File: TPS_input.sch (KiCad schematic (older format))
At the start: 3 parts, among them P48 CONN_1, P49 CONN_1, P50 CONN_1

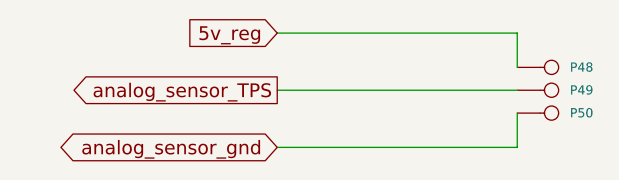
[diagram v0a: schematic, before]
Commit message: Removed LM1815 options. Now adaptive mode and square waves are the default,
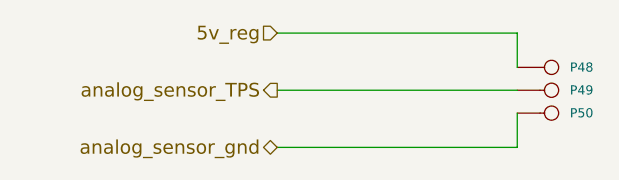
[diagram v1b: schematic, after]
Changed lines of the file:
@@
-EESchema Schematic File Version 1
-LIBS:power,./freeEMS_lib,device,conn,linear,regul,74xx,cmos4000,adc-dac,memory,xilinx,special,microcontrollers,dsp,microchip,analog_switches,motorola,texas,intel,audio,interface,digital-audio,philips,display,cypress,siliconi,contrib,valves,./freeEMS_1.cache
+EESchema Schematic File Version 2  date Fri 02 Jul 2010 02:24:35 PM ART
+LIBS:power
+LIBS:freeEMS_lib
+LIBS:device
+LIBS:conn
+LIBS:linear
+LIBS:regul
+LIBS:74xx
+LIBS:cmos4000
+LIBS:adc-dac
+LIBS:memory
+LIBS:xilinx
+LIBS:special
+LIBS:microcontrollers
+LIBS:dsp
+LIBS:microchip
+LIBS:analog_switches
+LIBS:motorola
+LIBS:texas
+LIBS:intel
+LIBS:audio
+LIBS:interface
+LIBS:digital-audio
+LIBS:philips
+LIBS:display
+LIBS:cypress
+LIBS:siliconi
+LIBS:contrib
+LIBS:valves
+LIBS:freeEMS_1-cache
 EELAYER 23  0
 EELAYER END
@@
 Sheet 38 41
 Title "freeEMS 1.0"
-Date "15 nov 2008"
+Date "2 jul 2010"
 Rev "A.20"
 Comp "diyefi.org"
@@
 U 1 1 48AA1ACF
 P 4450 2050
-F 0 "P50" H 4530 2050 40  0000 L C
-F 1 "CONN_1" H 4450 2105 30  0001 C C
-F 2 "1PIN" V 1130 2600 60  0001 C C
+F 0 "P50" H 4530 2050 40  0000 L CNN
+F 1 "CONN_1" H 4450 2105 30  0001 C CNN
+F 2 "1PIN" V 1130 2600 60  0001 C CNN
 	1    4450 2050
 	1    0    0    -1
@@
 U 1 1 48AA1ACC
 P 4450 1950
-F 0 "P49" H 4530 1950 40  0000 L C
-F 1 "CONN_1" H 4450 2005 30  0001 C C
-F 2 "1PIN" V 1130 2600 60  0001 C C
+F 0 "P49" H 4530 1950 40  0000 L CNN
+F 1 "CONN_1" H 4450 2005 30  0001 C CNN
+F 2 "1PIN" V 1130 2600 60  0001 C CNN
 	1    4450 1950
 	1    0    0    -1
@@
 U 1 1 48AA1AC9
 P 4450 1850
-F 0 "P48" H 4530 1850 40  0000 L C
-F 1 "CONN_1" H 4450 1905 30  0001 C C
-F 2 "1PIN" V 1130 2600 60  0001 C C
+F 0 "P48" H 4530 1850 40  0000 L CNN
+F 1 "CONN_1" H 4450 1905 30  0001 C CNN
+F 2 "1PIN" V 1130 2600 60  0001 C CNN
 	1    4450 1850
 	1    0    0    -1
@@
 Wire Wire Line
 	4300 1700 4300 1850
-Text GLabel 3250 1700 0    60   Input
+Text HLabel 3250 1700 0    60   Input ~ 0
 5v_reg
-Text GLabel 3250 2200 0    60   BiDi
+Text HLabel 3250 2200 0    60   BiDi ~ 0
 analog_sensor_gnd
-Text GLabel 3250 1950 0    60   Output
+Text HLabel 3250 1950 0    60   Output ~ 0
 analog_sensor_TPS
 $EndSCHEMATC

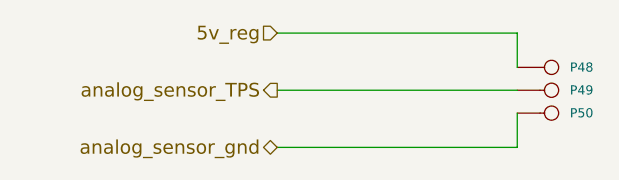
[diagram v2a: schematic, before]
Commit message: Implemented P&H, removed current sense circuitry, removed all unnecessary files from the repo
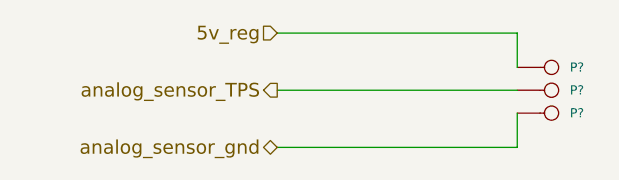
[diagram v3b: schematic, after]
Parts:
- renumbered P48 to P?, P49 to P?, P50 to P?
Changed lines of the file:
@@
-EESchema Schematic File Version 2  date Fri 02 Jul 2010 05:44:26 PM ART
+EESchema Schematic File Version 2  date Sat 03 Jul 2010 10:49:02 AM ART
 LIBS:power
 LIBS:freeEMS_lib
@@
 EELAYER END
 $Descr A4 11700 8267
-Sheet 38 41
+Sheet 39 41
 Title "freeEMS 1.0"
-Date "2 jul 2010"
-Rev "A.20"
+Date "3 jul 2010"
+Rev "A.08"
 Comp "diyefi.org"
 Comment1 "TPS_input.sch"
@@
 $EndDescr
 $Comp
-L CONN_1 P50
+L CONN_1 P?
 U 1 1 48AA1ACF
 P 4450 2050
-F 0 "P50" H 4530 2050 40  0000 L CNN
+F 0 "P?" H 4530 2050 40  0000 L CNN
 F 1 "CONN_1" H 4450 2105 30  0001 C CNN
 F 2 "1PIN" V 1130 2600 60  0001 C CNN
@@
 $EndComp
 $Comp
-L CONN_1 P49
+L CONN_1 P?
 U 1 1 48AA1ACC
 P 4450 1950
-F 0 "P49" H 4530 1950 40  0000 L CNN
+F 0 "P?" H 4530 1950 40  0000 L CNN
 F 1 "CONN_1" H 4450 2005 30  0001 C CNN
 F 2 "1PIN" V 1130 2600 60  0001 C CNN
@@
 $EndComp
 $Comp
-L CONN_1 P48
+L CONN_1 P?
 U 1 1 48AA1AC9
 P 4450 1850
-F 0 "P48" H 4530 1850 40  0000 L CNN
+F 0 "P?" H 4530 1850 40  0000 L CNN
 F 1 "CONN_1" H 4450 1905 30  0001 C CNN
 F 2 "1PIN" V 1130 2600 60  0001 C CNN
@@
 $EndComp
 Wire Wire Line
-	4300 2050 4300 2200
+	4300 2200 4300 2050
 Wire Wire Line
-	4300 2200 3250 2200
+	3250 2200 4300 2200
 Wire Wire Line
 	4300 1950 3250 1950

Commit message: Corrected ERC errors by fixing the custom FreeEMS components pinouts
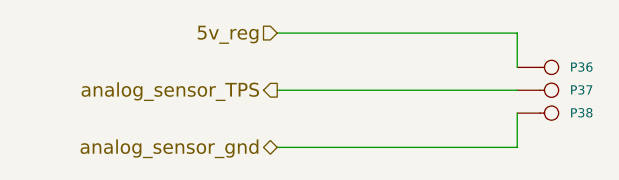
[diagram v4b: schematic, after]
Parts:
- gave numbers to parts that had none: 3
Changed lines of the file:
@@
-EESchema Schematic File Version 2  date Sat 03 Jul 2010 10:49:02 AM ART
+EESchema Schematic File Version 2  date Sat 03 Jul 2010 12:32:24 PM ART
 LIBS:power
 LIBS:freeEMS_lib
@@
 $EndDescr
 $Comp
-L CONN_1 P?
+L CONN_1 P38
 U 1 1 48AA1ACF
 P 4450 2050
-F 0 "P?" H 4530 2050 40  0000 L CNN
+F 0 "P38" H 4530 2050 40  0000 L CNN
 F 1 "CONN_1" H 4450 2105 30  0001 C CNN
 F 2 "1PIN" V 1130 2600 60  0001 C CNN
@@
 $EndComp
 $Comp
-L CONN_1 P?
+L CONN_1 P37
 U 1 1 48AA1ACC
 P 4450 1950
-F 0 "P?" H 4530 1950 40  0000 L CNN
+F 0 "P37" H 4530 1950 40  0000 L CNN
 F 1 "CONN_1" H 4450 2005 30  0001 C CNN
 F 2 "1PIN" V 1130 2600 60  0001 C CNN
@@
 $EndComp
 $Comp
-L CONN_1 P?
+L CONN_1 P36
 U 1 1 48AA1AC9
 P 4450 1850
-F 0 "P?" H 4530 1850 40  0000 L CNN
+F 0 "P36" H 4530 1850 40  0000 L CNN
 F 1 "CONN_1" H 4450 1905 30  0001 C CNN
 F 2 "1PIN" V 1130 2600 60  0001 C CNN
@@
 $EndComp
 Wire Wire Line
-	4300 2200 4300 2050
+	4300 2050 4300 2200
 Wire Wire Line
-	3250 2200 4300 2200
+	4300 2200 3250 2200
 Wire Wire Line
 	4300 1950 3250 1950
